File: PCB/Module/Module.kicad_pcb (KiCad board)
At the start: 2 copper layers, 34.2 x 34.2 mm, 28 parts, among them J1 SWD_Programmer, J2 Shield_Connector_Top_Right, J3 Shield_Connector_Bottom_Right, J4 Shield_Connector_Top_Left, J5 Shield_Connector_Bottom_Left, U1 PY32F002BF15P6TU, U2 PinHeaderTop, U3 PinHeaderRight, U4 PinHeaderBottom, U5 PinHeaderLeft

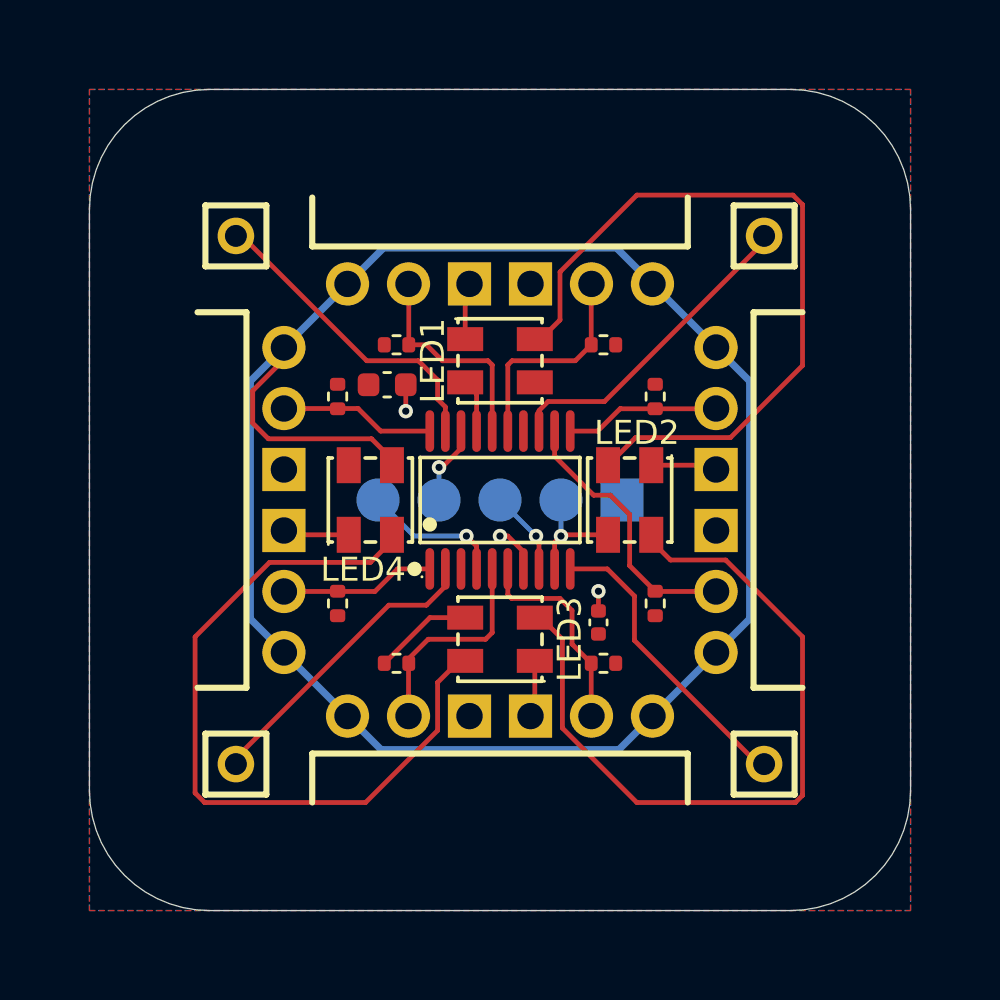
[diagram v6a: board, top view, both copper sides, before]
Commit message: Finish module, power supply and connector design, panel is wip
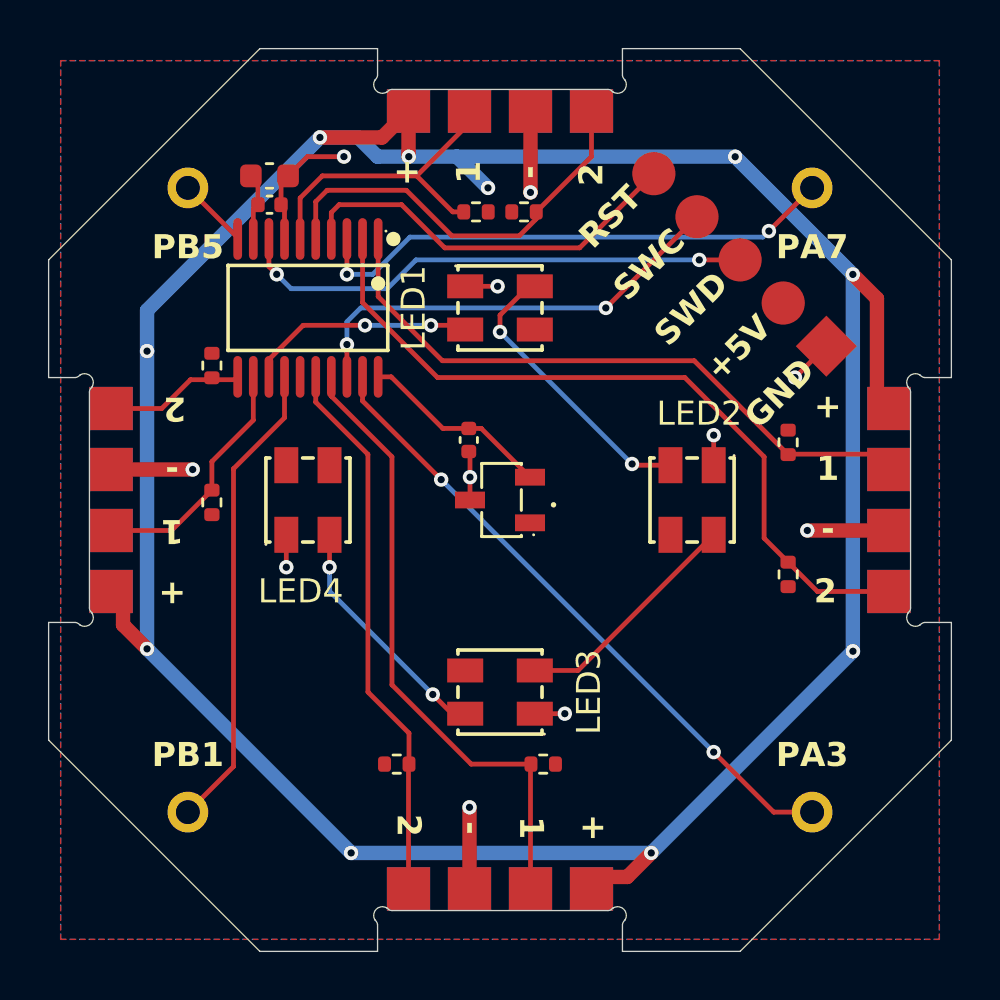
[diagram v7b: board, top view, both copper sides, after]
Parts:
- removed the REF** at (150.0, 82.7)
- removed the REF** at (150.0, 117.3)
- removed the REF** at (132.7, 100.0)
- removed the REF** at (167.3, 100.0)
- added C3: 10nF, Capacitor_SMD:C_0402_1005Metric, F.Cu at (148.7, 97.5)
- added REF**: Tab, PCM_kikit:Tab, F.Cu at (165.0, 85.0)
- added REF**: Tab, PCM_kikit:Tab, F.Cu at (165.0, 115.0)
- added REF**: Tab, PCM_kikit:Tab, F.Cu at (135.0, 115.0)
- added REF**: Tab, PCM_kikit:Tab, F.Cu at (135.0, 85.0)
- added U6: HallLinearSensor, CustomFootprints:HallLinearSensor, F.Cu at (150.0, 100.0)
- J1: moved to F.Cu
- J2: value Shield_Connector_Top_Right -> Conn_01x01; footprint CustomFootprints:HDR-TH_1P-V-F-1 -> CustomFootprints:ShieldConnector
- J3: value Shield_Connector_Bottom_Right -> Conn_01x01; footprint CustomFootprints:HDR-TH_1P-V-F-1 -> CustomFootprints:ShieldConnector
- J4: value Shield_Connector_Top_Left -> Conn_01x01; footprint CustomFootprints:HDR-TH_1P-V-F-1 -> CustomFootprints:ShieldConnector
- J5: value Shield_Connector_Bottom_Left -> Conn_01x01; footprint CustomFootprints:HDR-TH_1P-V-F-1 -> CustomFootprints:ShieldConnector
- PinHeaderBottom1: renamed from U4; value PinHeaderBottom -> PinHeader; footprint CustomFootprints:01x06_PinHeader_Angled -> CustomFootprints:01x04_PinPads
- PinHeaderLeft1: renamed from U5; value PinHeaderLeft -> PinHeader; footprint CustomFootprints:01x06_PinHeader_Angled -> CustomFootprints:01x04_PinPads
- PinHeaderRight1: renamed from U3; value PinHeaderRight -> PinHeader; footprint CustomFootprints:01x06_PinHeader_Angled -> CustomFootprints:01x04_PinPads
- PinHeaderTop1: renamed from U2; value PinHeaderTop -> PinHeader; footprint CustomFootprints:01x06_PinHeader_Angled -> CustomFootprints:01x04_PinPads
- moved J2 24.3 mm to (136.8, 87.0)
- moved J3 24.3 mm to (136.8, 113.0)
- moved J4 23.9 mm to (162.8, 87.0)
- moved J5 23.9 mm to (162.8, 113.0)
- moved C2 22.1 mm to (140.4, 87.7), turned to 180 degrees
- moved J1 14.1 mm to (160.0, 90.0), turned to 135 degrees
- moved U1 11.3 mm to (142.0, 92.0), turned to 180 degrees
- moved R7 11.2 mm to (138.0, 94.4), turned to -90 degrees
- moved C1 9.98 mm to (140.4, 86.5)
- moved R5 9.58 mm to (145.7, 111.0), turned to 0 degrees
- moved R3 9.25 mm to (162.0, 103.1), turned to 90 degrees
- moved R4 8.70 mm to (162.0, 97.6), turned to -90 degrees
- moved R1 7.67 mm to (151.0, 88.0)
- moved R2 7.67 mm to (149.0, 88.0)
- moved R6 7.41 mm to (151.8, 111.0), turned to 180 degrees
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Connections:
- J2 pad 1: /ShieldTopRight -> /ShieldTopLeft
- J3 pad 1: /ShieldBottomRight -> /ShieldBottomLeft
- J4 pad 1: /ShieldTopLeft_ADC -> /ShieldTopRight
- J5 pad 1: /ShieldBottomLeft_ADC -> /ShieldBottomRight
- PinHeaderBottom1 pad 4: GND -> /DataBottom2
- PinHeaderLeft1 pad 4: GND -> /DataLeft2
- PinHeaderRight1 pad 4: GND -> /DataRight2
- PinHeaderTop1 pad 4: GND -> /DataTop2
- U1 pad 1: /DataLeft2 -> /DataRight1
- U1 pad 10: /ShieldBottomRight -> /ShieldTopLeft
- U1 pad 11: /DataRight2 -> /DataLeft2
- U1 pad 12: /DataRight1 -> /DataLeft1
- U1 pad 13: /ShieldTopRight -> /LedIn
- U1 pad 14: unconnected-(U1-PB1-Pad14) -> /ShieldBottomLeft
- U1 pad 15: /DataTop1 -> unconnected-(U1-PB0-Pad15)
- U1 pad 16: /DataTop2 -> /DataBottom2
- U1 pad 17: /LedIn -> /DataBottom1
- U1 pad 19: /ShieldTopLeft_ADC -> /ShieldBottomRight
- U1 pad 2: /ShieldBottomLeft_ADC -> /DataRight2
- U1 pad 20: /DataLeft1 -> /HallAdc
- U1 pad 3: unconnected-(U1-PA7-Pad3) -> /ShieldTopRight
- U1 pad 5: /DataBottom1 -> /DataTop2
- U1 pad 6: /DataBottom2 -> /DataTop1
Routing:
- net +5V: track 90.2 -> 123.4 mm, vias 1 -> 10
- net /DataRight2: track 6.47 -> 31.5 mm
- net Net-(LED2-DOUT): track 31.4 -> 9.79 mm
- net Net-(LED3-DOUT): track 31.6 -> 10.1 mm, vias 0 -> 2
- net /ShieldBottomLeft: track 0.00 -> 19.8 mm
- net Net-(LED1-DOUT): track 31.5 -> 12.0 mm, vias 0 -> 2
- net /SWD: track 3.54 -> 21.7 mm, vias 1 -> 2
- net /DataBottom1: track 8.80 -> 26.2 mm
- net /SWC: track 3.32 -> 18.7 mm, vias 1 -> 2
- net /DataRight1: track 11.4 -> 26.7 mm
- net GND: track 13.2 -> 28.1 mm, vias 3 -> 11
- net /DataBottom2: track 8.25 -> 22.9 mm
- net /ShieldBottomRight: track 12.8 -> 26.8 mm, vias 0 -> 2
- net /ShieldTopLeft_ADC: track 13.1 -> 0.00 mm
- net /ShieldBottomLeft_ADC: track 12.7 -> 0.00 mm
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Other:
- board size 34.2 x 34.2 mm -> 37.6 x 37.6 mm
- board text added: "+"
- board text added: "-"
- board text added: "1"
- board text added: "2"
- board text added: "5V"
- board text added: "D1"
- board text added: "D2"
- board text added: "PA3"
- board text added: "PA7"
- board text added: "PB1"
- board text added: "PB5"
- board text added: "Pogo"
- board text removed: "PCB"
- board text removed: "Pogo Pins"

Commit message: Finish panel script
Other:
- board text added: "LED1"
- board text added: "LED2"
- board text added: "LED3"
- board text added: "LED4"
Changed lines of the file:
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@@
 		(sheetname "Root")
 		(sheetfile "Module.kicad_sch")
-		(attr smd exclude_from_bom)
+		(attr smd exclude_from_bom dnp)
 		(fp_text user "${REFERENCE}"
 			(at 0 2.5 0)
@@
 		(sheetname "Root")
 		(sheetfile "Module.kicad_sch")
-		(attr smd exclude_from_bom)
+		(attr smd exclude_from_bom dnp)
 		(fp_text user "REF**"
 			(at 0 12.8 -90)
@@
 		)
 		(fp_text user "KIKIT: width: 5mm"
-			(at -5.5 0 315)
+			(at -5.5 0 -45)
 			(layer "Dwgs.User")
 			(effects
@@
 		(tags "resistor")
 		(property "Reference" "R5"
-			(at 0 -1.17 360)
+			(at 0 -1.17 0)
 			(layer "F.SilkS")
 			(hide yes)
@@
 		)
 		(property "Value" "10k"
-			(at 0 1.17 360)
+			(at 0 1.17 0)
 			(layer "F.Fab")
 			(effects
@@
 		)
 		(fp_text user "${REFERENCE}"
-			(at 0 0 360)
+			(at 0 0 0)
 			(layer "F.Fab")
 			(effects
@@
 		(sheetname "Root")
 		(sheetfile "Module.kicad_sch")
-		(attr smd exclude_from_bom)
+		(attr smd exclude_from_bom dnp)
 		(fp_text user "REF**"
 			(at 0 12.8 90)
@@
 			(at 3.7 0 -90)
 			(layer "F.SilkS")
+			(hide yes)
 			(effects
 				(font
@@
 			(at 3.6 0.3 0)
 			(layer "F.SilkS")
+			(hide yes)
 			(effects
 				(font
@@
 		)
 		(fp_text user "KIKIT: width: 5mm"
-			(at -5.5 0 225)
+			(at -5.5 0 -135)
 			(layer "Dwgs.User")
 			(effects
@@
 			(at 3.8 0.3 180)
 			(layer "F.SilkS")
+			(hide yes)
 			(effects
 				(font
@@
 		(sheetname "Root")
 		(sheetfile "Module.kicad_sch")
-		(attr smd exclude_from_bom)
+		(attr smd exclude_from_bom dnp)
 		(fp_text user "${REFERENCE}"
 			(at 0 2.5 180)
@@
 		(tags "resistor")
 		(property "Reference" "R2"
-			(at 0 -1.17 360)
+			(at 0 -1.17 0)
 			(layer "F.SilkS")
 			(hide yes)
@@
 		)
 		(property "Value" "10k"
-			(at 0 1.17 360)
+			(at 0 1.17 0)
 			(layer "F.Fab")
 			(effects
@@
 		)
 		(fp_text user "${REFERENCE}"
-			(at -0.01 0 360)
+			(at -0.01 0 0)
 			(layer "F.Fab")
 			(effects
@@
 			(at 3.6 0 90)
 			(layer "F.SilkS")
+			(hide yes)
 			(effects
 				(font
@@
 		)
 	)
+	(gr_text "LED2"
+		(at 158.3 96.4 0)
+		(layer "F.SilkS")
+		(effects
+			(font
+				(size 1 1)
+				(thickness 0.15)
+			)
+		)
+	)
 	(gr_text "+"
 		(at 163.65 96.1 0)
@@
 		)
 	)
+	(gr_text "LED4"
+		(at 141.7 103.8 0)
+		(layer "F.SilkS")
+		(effects
+			(font
+				(size 1 1)
+				(thickness 0.15)
+			)
+		)
+	)
 	(gr_text "2"
 		(at 163.55 103.8 0)
@@
 		)
 	)
+	(gr_text "LED3"
+		(at 153.7 108 90)
+		(layer "F.SilkS")
+		(effects
+			(font
+				(size 1 1)
+				(thickness 0.15)
+			)
+		)
+	)
 	(gr_text "1"
 		(at 136.35 101.3 180)
@@
 			)
 		)
+	)
+	(gr_text "LED1"
+		(at 146.4 92 90)
+		(layer "F.SilkS")
+		(effects
+			(font
+				(size 1 1)
+				(thickness 0.15)
+			)
+		)
